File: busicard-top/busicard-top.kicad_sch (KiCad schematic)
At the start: 12 parts

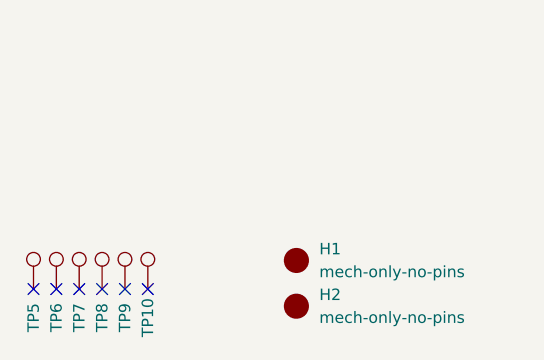
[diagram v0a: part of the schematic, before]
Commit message: busicard-top: enlarge battery opening
move all mount points 0.5mm towards edges
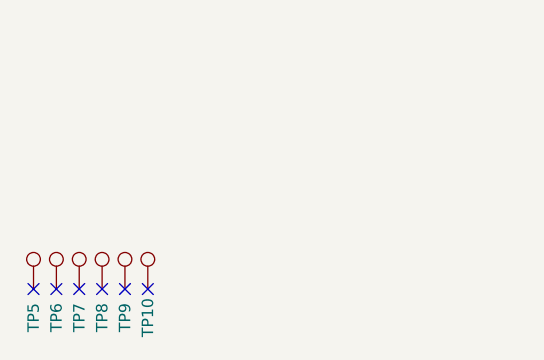
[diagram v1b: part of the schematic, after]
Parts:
- removed H1, H2: mech-only-no-pins, lib:JLC_ASSEMBLY_HOLE, symbol lib:mech-only-no-pins
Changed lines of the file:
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@@
-	)
-	(symbol
-		(lib_id "lib:mech-only-no-pins")
-		(at 214.63 171.45 0)
-		(unit 1)
-		(exclude_from_sim no)
-		(in_bom yes)
-		(on_board yes)
-		(dnp no)
-		(fields_autoplaced yes)
-		(property "Reference" "H1"
-			(at 217.17 170.1799 0)
-			(effects
-				(font
-					(size 1.27 1.27)
-				)
-				(justify left)
-			)
-		)
-		(property "Value" "mech-only-no-pins"
-			(at 217.17 172.7199 0)
-			(effects
-				(font
-					(size 1.27 1.27)
-				)
-				(justify left)
-			)
-		)
-		(property "Footprint" "lib:JLC_ASSEMBLY_HOLE"
-			(at 214.63 171.45 0)
-			(effects
-				(font
-					(size 1.27 1.27)
-				)
-				(hide yes)
-			)
-		)
-		(property "Datasheet" ""
-			(at 214.63 171.45 0)
-			(effects
-				(font
-					(size 1.27 1.27)
-				)
-				(hide yes)
-			)
-		)
-		(property "Description" ""
-			(at 214.63 171.45 0)
-			(effects
-				(font
-					(size 1.27 1.27)
-				)
-				(hide yes)
-			)
-		)
-		(instances
-			(project "busicard-top"
-				(path "/ecc7afd1-5dad-4e8f-989a-38019625b19d"
-					(reference "H1")
-					(unit 1)
-				)
-			)
-		)
 	)
 	(symbol
@@
 					(unit 1)
 				)
-			)
-		)
-	)
-	(symbol
-		(lib_id "lib:mech-only-no-pins")
-		(at 214.63 176.53 0)
-		(unit 1)
-		(exclude_from_sim no)
-		(in_bom yes)
-		(on_board yes)
-		(dnp no)
-		(fields_autoplaced yes)
-		(property "Reference" "H2"
-			(at 217.17 175.2599 0)
-			(effects
-				(font
-					(size 1.27 1.27)
-				)
-				(justify left)
-			)
-		)
-		(property "Value" "mech-only-no-pins"
-			(at 217.17 177.7999 0)
-			(effects
-				(font
-					(size 1.27 1.27)
-				)
-				(justify left)
-			)
-		)
-		(property "Footprint" "lib:JLC_ASSEMBLY_HOLE"
-			(at 214.63 176.53 0)
-			(effects
-				(font
-					(size 1.27 1.27)
-				)
-				(hide yes)
-			)
-		)
-		(property "Datasheet" ""
-			(at 214.63 176.53 0)
-			(effects
-				(font
-					(size 1.27 1.27)
-				)
-				(hide yes)
-			)
-		)
-		(property "Description" ""
-			(at 214.63 176.53 0)
-			(effects
-				(font
-					(size 1.27 1.27)
-				)
-				(hide yes)
-			)
-		)
-		(instances
-			(project "busicard-top"
-				(path "/ecc7afd1-5dad-4e8f-989a-38019625b19d"
-					(reference "H2")
-					(unit 1)
-				)

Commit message: Add assembly holes and batch number on silkscreen
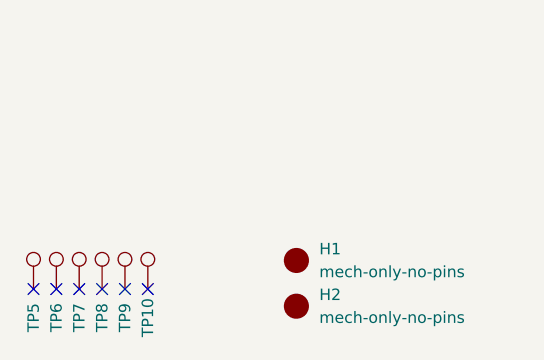
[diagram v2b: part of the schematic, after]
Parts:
- added H1, H2: mech-only-no-pins, lib:JLC_ASSEMBLY_HOLE, symbol lib:mech-only-no-pins
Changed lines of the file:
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@@
+	)
+	(symbol
+		(lib_id "lib:mech-only-no-pins")
+		(at 214.63 171.45 0)
+		(unit 1)
+		(exclude_from_sim no)
+		(in_bom yes)
+		(on_board yes)
+		(dnp no)
+		(fields_autoplaced yes)
+		(property "Reference" "H1"
+			(at 217.17 170.1799 0)
+			(effects
+				(font
+					(size 1.27 1.27)
+				)
+				(justify left)
+			)
+		)
+		(property "Value" "mech-only-no-pins"
+			(at 217.17 172.7199 0)
+			(effects
+				(font
+					(size 1.27 1.27)
+				)
+				(justify left)
+			)
+		)
+		(property "Footprint" "lib:JLC_ASSEMBLY_HOLE"
+			(at 214.63 171.45 0)
+			(effects
+				(font
+					(size 1.27 1.27)
+				)
+				(hide yes)
+			)
+		)
+		(property "Datasheet" ""
+			(at 214.63 171.45 0)
+			(effects
+				(font
+					(size 1.27 1.27)
+				)
+				(hide yes)
+			)
+		)
+		(property "Description" ""
+			(at 214.63 171.45 0)
+			(effects
+				(font
+					(size 1.27 1.27)
+				)
+				(hide yes)
+			)
+		)
+		(instances
+			(project "busicard-top"
+				(path "/ecc7afd1-5dad-4e8f-989a-38019625b19d"
+					(reference "H1")
+					(unit 1)
+				)
+			)
+		)
 	)
 	(symbol
@@
 					(unit 1)
 				)
+			)
+		)
+	)
+	(symbol
+		(lib_id "lib:mech-only-no-pins")
+		(at 214.63 176.53 0)
+		(unit 1)
+		(exclude_from_sim no)
+		(in_bom yes)
+		(on_board yes)
+		(dnp no)
+		(fields_autoplaced yes)
+		(property "Reference" "H2"
+			(at 217.17 175.2599 0)
+			(effects
+				(font
+					(size 1.27 1.27)
+				)
+				(justify left)
+			)
+		)
+		(property "Value" "mech-only-no-pins"
+			(at 217.17 177.7999 0)
+			(effects
+				(font
+					(size 1.27 1.27)
+				)
+				(justify left)
+			)
+		)
+		(property "Footprint" "lib:JLC_ASSEMBLY_HOLE"
+			(at 214.63 176.53 0)
+			(effects
+				(font
+					(size 1.27 1.27)
+				)
+				(hide yes)
+			)
+		)
+		(property "Datasheet" ""
+			(at 214.63 176.53 0)
+			(effects
+				(font
+					(size 1.27 1.27)
+				)
+				(hide yes)
+			)
+		)
+		(property "Description" ""
+			(at 214.63 176.53 0)
+			(effects
+				(font
+					(size 1.27 1.27)
+				)
+				(hide yes)
+			)
+		)
+		(instances
+			(project "busicard-top"
+				(path "/ecc7afd1-5dad-4e8f-989a-38019625b19d"
+					(reference "H2")
+					(unit 1)
+				)
